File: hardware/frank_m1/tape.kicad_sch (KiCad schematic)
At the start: 11 parts, among them Q1 BC850, Q2 BC850

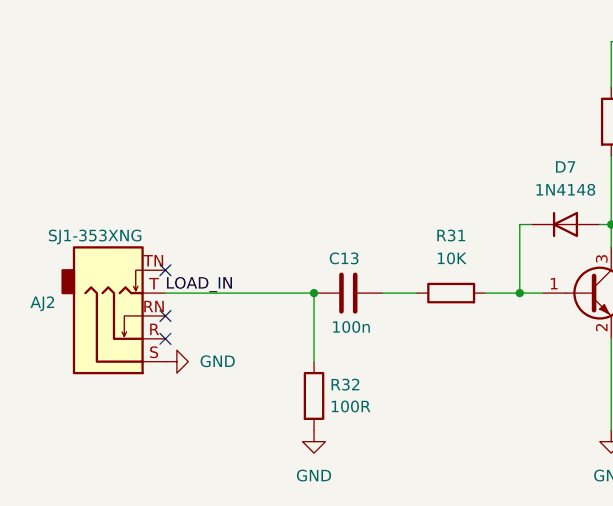
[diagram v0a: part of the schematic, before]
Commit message: Fixed tape loading bug on all PCBs
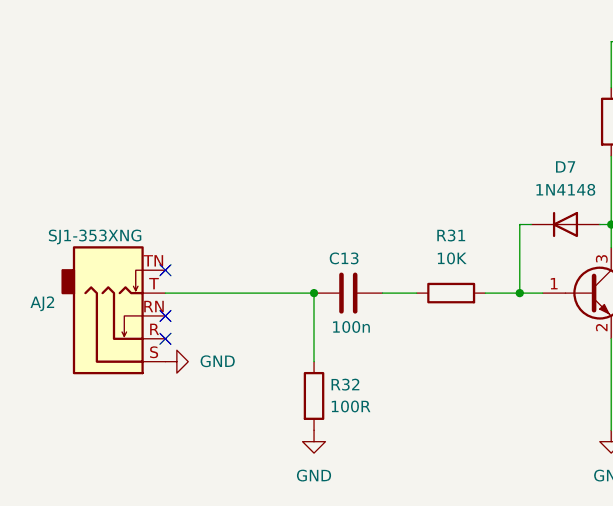
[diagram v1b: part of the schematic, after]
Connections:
- net LOAD_IN: no longer AJ2.T, C13.1, R32.1
- new net: AJ2.T, C13.1, R32.1
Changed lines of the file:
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@@
 	(title_block
 		(title "FRANK M1")
-		(date "2025-03-03")
-		(rev "1.14")
+		(date "2025-03-16")
+		(rev "1.15")
 		(company "Mikhail Matveev")
 		(comment 1 "https://github.com/xtremespb/frank")
@@
 		)
 	)
-	(label "LOAD_IN"
-		(at 49.53 72.39 0)
-		(effects
-			(font
-				(size 1.27 1.27)
-			)
-			(justify left bottom)
-		)
-	)

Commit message: Bugfixes
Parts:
- Q1, Q2: footprint Package_TO_SOT_SMD:SOT-23 -> FRANK:SOT-23
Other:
- note removed: "This schematics is used to load data from external audio source, e.g. tape."
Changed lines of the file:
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@@
 		(comment 1 "https://github.com/xtremespb/frank")
-	)
-	(text "This schematics is used to load data from\nexternal audio source, e.g. tape."
-		(exclude_from_sim no)
-		(at 38.1 27.178 0)
-		(effects
-			(font
-				(size 1.27 1.27)
-			)
-			(justify left)
-		)
 	)
 	(junction
@@
 			)
 		)
-		(property "Footprint" "Package_TO_SOT_SMD:SOT-23"
+		(property "Footprint" "FRANK:SOT-23"
 			(at 101.6 74.295 0)
 			(effects
@@
 			)
 		)
-		(property "Footprint" "Package_TO_SOT_SMD:SOT-23"
+		(property "Footprint" "FRANK:SOT-23"
 			(at 119.38 66.675 0)
 			(effects

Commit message: FRANK M1 1.16 WIP
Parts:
- renumbered AJ2 to J11
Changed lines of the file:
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@@
 	(title_block
 		(title "FRANK M1")
-		(date "2025-03-16")
-		(rev "1.15")
+		(date "2025-03-26")
+		(rev "1.16")
 		(company "Mikhail Matveev")
 		(comment 1 "https://github.com/xtremespb/frank")
@@
 		(on_board yes)
 		(dnp no)
-		(property "Reference" "AJ2"
+		(property "Reference" "J11"
 			(at 37.3381 73.4603 0)
 			(effects
@@
 			(project "38NJU24"
 				(path "/8c0b3d8b-46d3-4173-ab1e-a61765f77d61/599e2208-d0f7-4f1d-beb8-3b4e6272cb10"
-					(reference "AJ2")
-					(unit 1)
-				)
+					(reference "J11")
+					(unit 1)
+				)

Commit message: Minor updates
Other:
- moved on the sheet: C12, C13, D7, J11, Q1, Q2, R28, R29, R30, R31, R32
